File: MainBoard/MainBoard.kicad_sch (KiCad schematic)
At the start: 30 parts, among them J1 Conn_01x20, J11-L-FRONT1 Screw_Terminal_01x02, J12-L-REAR1 Screw_Terminal_01x02, J13-R-FRONT1 Screw_Terminal_01x02, J14-R-REAR1 Screw_Terminal_01x02, J2 Conn_01x12, J3 Conn_01x10, J4 Conn_01x07, SW1 SW_Push

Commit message: 전원배선완료
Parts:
- removed MP1584EN_OUT: Conn_01x06, symbol Connector_Generic:Conn_01x06
- added C7, C8, C9: 100nF, Capacitor_THT:C_Disc_D5.0mm_W2.5mm_P5.00mm, symbol Device:C
- added MP1584EN_OUT1: Conn_01x06, Connector_PinSocket_2.54mm:PinSocket_1x06_P2.54mm_Vertical, symbol Connector_Generic:Conn_01x06
- C1: value 100uF -> 470uF
- MP1584EN_IN1: renamed from MP1584EN_IN; footprint (none) -> Connector_PinSocket_2.54mm:PinSocket_1x06_P2.54mm_Vertical
- renumbered MINI360_IN to MINI360_IN1, MINI360_IN1 to MINI360_OUT1
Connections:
- net 5V0: now also C7.1, MP1584EN_OUT1.1 (Pin_1), MP1584EN_OUT1.2 (Pin_2), MP1584EN_OUT1.3 (Pin_3)
- net GND: now also MINI360_OUT1.3 (Pin_3), MINI360_OUT1.4 (Pin_4), C7.2, C8.2, C9.2, MP1584EN_OUT1.4 (Pin_4), MP1584EN_OUT1.5 (Pin_5), MP1584EN_OUT1.6 (Pin_6); no longer MINI360_OUT1.1 (Pin_1), MINI360_OUT1.2 (Pin_2)
- net VCC: now also MINI360_OUT1.1 (Pin_1), MINI360_OUT1.2 (Pin_2), C8.1, C9.1; no longer MINI360_OUT1.3 (Pin_3), MINI360_OUT1.4 (Pin_4)
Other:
- moved on the sheet: BT1, D1, MINI360_IN1, MINI360_OUT1, MP1584EN_IN1, R3, SW1

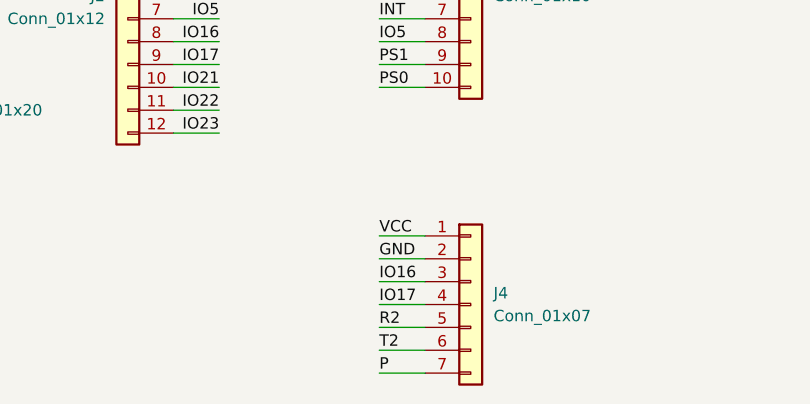
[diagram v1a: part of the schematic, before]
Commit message: drv8833_R배선필요
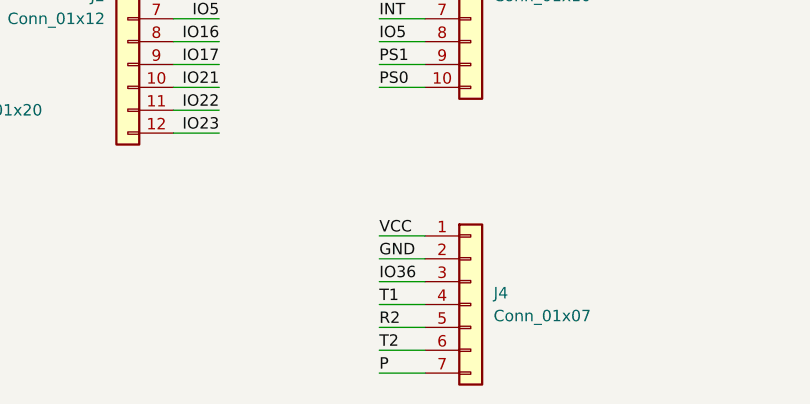
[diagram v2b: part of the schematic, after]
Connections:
- net IO16: no longer J4.3 (Pin_3)
- net IO17: no longer J4.4 (Pin_4)
- net IO36: now also J4.3 (Pin_3)
- new net T1: J4.4 (Pin_4)
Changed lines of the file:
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@@
 		)
 	)
-	(label "IO16"
+	(label "IO36"
 		(at 134.62 166.37 0)
 		(effects
@@
 		)
 	)
-	(label "IO17"
+	(label "T1"
 		(at 134.62 168.91 0)
 		(effects
